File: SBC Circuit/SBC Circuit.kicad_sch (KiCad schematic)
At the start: 20 parts, among them J3 Conn_01x06_Pin, SW1 RESET, U1 MC68000FN, U11 MC34064P, U2 XC9572XL, X1 SG-531

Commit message: Finish power and IO circuit
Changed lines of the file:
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@@
     (effects (font (size 1.27 1.27)) (justify left bottom))
-  )
-  (label "n0" (at 196.85 129.54 180) (fields_autoplaced)
-    (effects (font (size 1.27 1.27)) (justify right bottom))
-    (property "Netclass" "signal" (at 196.85 130.81 0)
-      (effects (font (size 1.27 1.27) italic) (justify right) hide)
-    )
   )
   (label "tms" (at 106.68 180.34 270) (fields_autoplaced)

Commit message: Begin final PCB placement
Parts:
- added TP5: ~{AS}, TestPoint:TestPoint_Keystone_5000-5004_Miniature, symbol Connector:TestPoint
- added TP6: ~{DTACK}, TestPoint:TestPoint_Keystone_5000-5004_Miniature, symbol Connector:TestPoint
- renumbered R3 to R4, R4 to R5
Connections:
- net as: now also TP5.1
- net dtack: now also TP6.1
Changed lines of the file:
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@@
   (title_block
     (title "MICROPROCESSOR & ADDRESS ROUTER")
-    (date "2024-01-24")
-    (rev "0.4")
+    (date "2024-01-25")
+    (rev "0.5")
     (company "LeTourneau University")
     (comment 1 "Richard Homan")
@@
     (stroke (width 0) (type default))
   )
+  (bus_entry (at 22.86 95.25) (size 2.54 2.54)
+    (stroke (width 0) (type default))
+  )
   (bus_entry (at 71.12 162.56) (size 2.54 2.54)
     (stroke (width 0) (type default))
@@
     (stroke (width 0) (type default))
   )
+  (bus_entry (at 22.86 100.33) (size 2.54 2.54)
+    (stroke (width 0) (type default))
+  )
   (bus_entry (at 264.16 63.5) (size -2.54 2.54)
     (stroke (width 0) (type default))
@@
     (stroke (width 0) (type default))
   )
+  (wire (pts (xy 25.4 102.87) (xy 31.75 102.87))
+    (stroke (width 0) (type default))
+  )
   (bus (pts (xy 187.96 69.85) (xy 187.96 72.39))
     (stroke (width 0) (type default))
@@
     (stroke (width 0) (type default))
   )
+  (wire (pts (xy 25.4 97.79) (xy 31.75 97.79))
+    (stroke (width 0) (type default))
+  )
   (wire (pts (xy 213.36 15.24) (xy 218.44 15.24))
     (stroke (width 0) (type default))
@@
   )
   (wire (pts (xy 93.98 180.34) (xy 96.52 180.34))
+    (stroke (width 0) (type default))
+  )
+  (bus (pts (xy 22.86 95.25) (xy 22.86 100.33))
     (stroke (width 0) (type default))
   )
@@
     (effects (font (size 1.27 1.27)) (justify left bottom))
   )
+  (label "{as,uds,lds,rw,dtack,berr}" (at 22.86 95.25 270) (fields_autoplaced)
+    (effects (font (size 1.27 1.27)) (justify right bottom))
+    (property "Netclass" "bus" (at 24.13 95.25 90)
+      (effects (font (size 1.27 1.27) italic) (justify right) hide)
+    )
+  )
   (label "fc2" (at 121.92 115.57 0) (fields_autoplaced)
     (effects (font (size 1.27 1.27)) (justify left bottom))
@@
     (effects (font (size 1.27 1.27)) (justify left bottom))
   )
+  (label "dtack" (at 31.75 102.87 180)
+    (effects (font (size 1.27 1.27)) (justify right bottom))
+  )
   (label "data11" (at 251.46 137.16 0) (fields_autoplaced)
     (effects (font (size 1.27 1.27)) (justify left bottom))
@@
   (label "addr4" (at 251.46 58.42 0) (fields_autoplaced)
     (effects (font (size 1.27 1.27)) (justify left bottom))
+  )
+  (label "as" (at 31.75 97.79 180)
+    (effects (font (size 1.27 1.27)) (justify right bottom))
   )
   (global_label "clk" (shape input) (at 36.83 35.56 0) (fields_autoplaced)
@@
   (symbol (lib_id "Device:R") (at 119.38 34.29 0) (unit 1)
     (in_bom yes) (on_board yes) (dnp no)
-    (property "Reference" "R4" (at 121.92 33.02 0)
+    (property "Reference" "R5" (at 121.92 33.02 0)
       (effects (font (size 1.27 1.27)) (justify left))
     )
@@
       (project "SBC Circuit"
         (path "/3db026c4-f98d-4c94-ab2a-d9924b8daebe"
-          (reference "R4") (unit 1)
+          (reference "R5") (unit 1)
         )
       )
@@
   (symbol (lib_id "Device:R") (at 93.98 34.29 0) (mirror y) (unit 1)
     (in_bom yes) (on_board yes) (dnp no)
-    (property "Reference" "R3" (at 91.44 33.02 0)
+    (property "Reference" "R4" (at 91.44 33.02 0)
       (effects (font (size 1.27 1.27)) (justify left))
     )
@@
       (project "SBC Circuit"
         (path "/3db026c4-f98d-4c94-ab2a-d9924b8daebe"
-          (reference "R3") (unit 1)
+          (reference "R4") (unit 1)
         )
       )
@@
     )
   )
+  (symbol (lib_id "Connector:TestPoint") (at 31.75 102.87 270) (unit 1)
+    (in_bom yes) (on_board yes) (dnp no) (fields_autoplaced)
+    (property "Reference" "TP6" (at 36.83 101.6 90)
+      (effects (font (size 1.27 1.27)) (justify left))
+    )
+    (property "Value" "~{DTACK}" (at 36.83 104.14 90)
+      (effects (font (size 1.27 1.27)) (justify left))
+    )
+    (property "Footprint" "TestPoint:TestPoint_Keystone_5000-5004_Miniature" (at 31.75 107.95 0)
+      (effects (font (size 1.27 1.27)) hide)
+    )
+    (property "Datasheet" "~" (at 31.75 107.95 0)
+      (effects (font (size 1.27 1.27)) hide)
+    )
+    (pin "1")
+    (instances
+      (project "SBC Circuit"
+        (path "/3db026c4-f98d-4c94-ab2a-d9924b8daebe"
+          (reference "TP6") (unit 1)
+        )
+      )
+    )
+  )
   (symbol (lib_id "power:+5V") (at 29.21 27.94 0) (unit 1)
     (in_bom yes) (on_board yes) (dnp no) (fields_autoplaced)
@@
         )
       )
+    )
+  )
+  (symbol (lib_id "Connector:TestPoint") (at 31.75 97.79 270) (unit 1)
+    (in_bom yes) (on_board yes) (dnp no) (fields_autoplaced)
+    (property "Reference" "TP5" (at 36.83 96.52 90)
+      (effects (font (size 1.27 1.27)) (justify left))
+    )
+    (property "Value" "~{AS}" (at 36.83 99.06 90)
+      (effects (font (size 1.27 1.27)) (justify left))
+    )
+    (property "Footprint" "TestPoint:TestPoint_Keystone_5000-5004_Miniature" (at 31.75 102.87 0)
+      (effects (font (size 1.27 1.27)) hide)
+    )
+    (property "Datasheet" "~" (at 31.75 102.87 0)
+      (effects (font (size 1.27 1.27)) hide)
+    )
+    (pin "1")
+    (instances
+      (project "SBC Circuit"
+        (path "/3db026c4-f98d-4c94-ab2a-d9924b8daebe"
+          (reference "TP5") (unit 1)
+        )
+      )

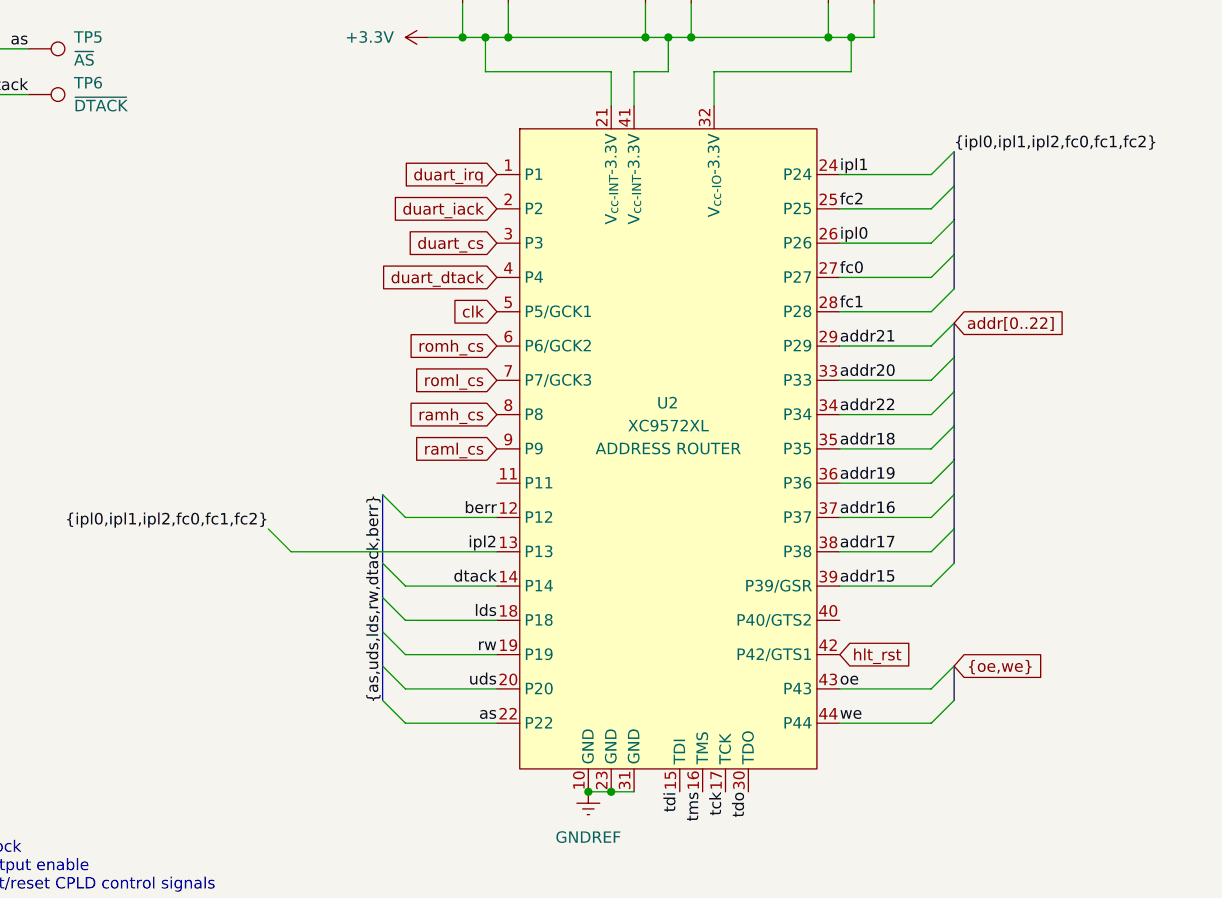
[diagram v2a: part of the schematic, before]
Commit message: Finish DUART lines
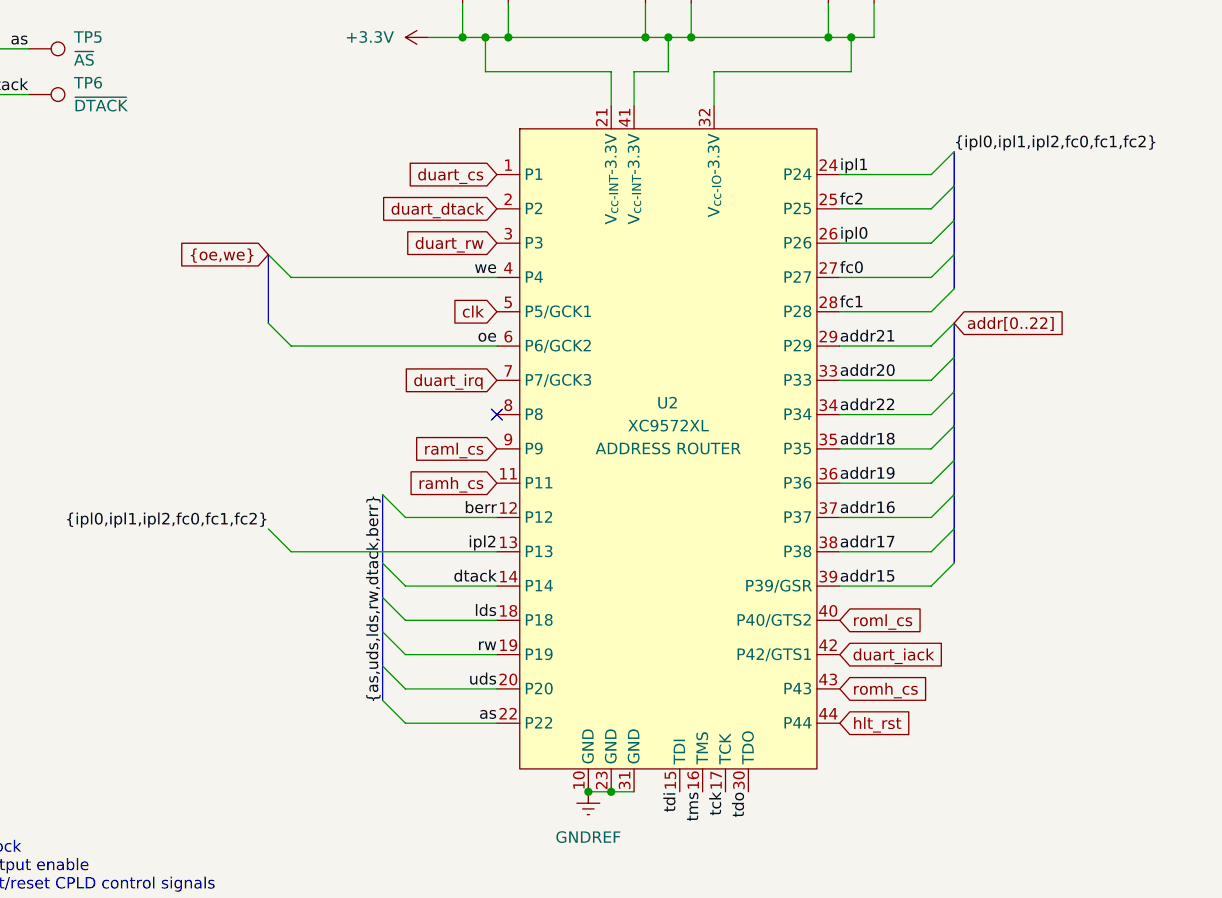
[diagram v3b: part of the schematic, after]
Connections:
- net duart_cs: now also U2.1 (P1); no longer U2.3 (P3)
- net duart_dtack: now also U2.2 (P2); no longer U2.4 (P4)
- net duart_iack: now also U2.42 (P42/GTS1); no longer U2.2 (P2)
- net duart_irq: now also U2.7 (P7/GCK3); no longer U2.1 (P1)
- net hlt_rst: now also U2.44 (P44); no longer U2.42 (P42/GTS1)
- net oe: now also U2.6 (P6/GCK2); no longer U2.43 (P43)
- net ramh_cs: now also U2.11 (P11); no longer U2.8 (P8)
- net romh_cs: now also U2.43 (P43); no longer U2.6 (P6/GCK2)
- net roml_cs: now also U2.40 (P40/GTS2); no longer U2.7 (P7/GCK3)
- net we: now also U2.4 (P4); no longer U2.44 (P44)
- new net duart_rw: U2.3 (P3)
- no-connect marks 3 -> 4
